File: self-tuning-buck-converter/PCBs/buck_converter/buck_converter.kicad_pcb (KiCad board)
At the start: 2 copper layers, 91.2 x 82.6 mm, 54 parts, among them Q1 NMOS, U1 TLO84CN, U2 OPA2830, U3 LT1999-50, U4 LD1117V50, U6 ESP32-DEVKITC-32D, U7 IR2125, U8 MAX11644

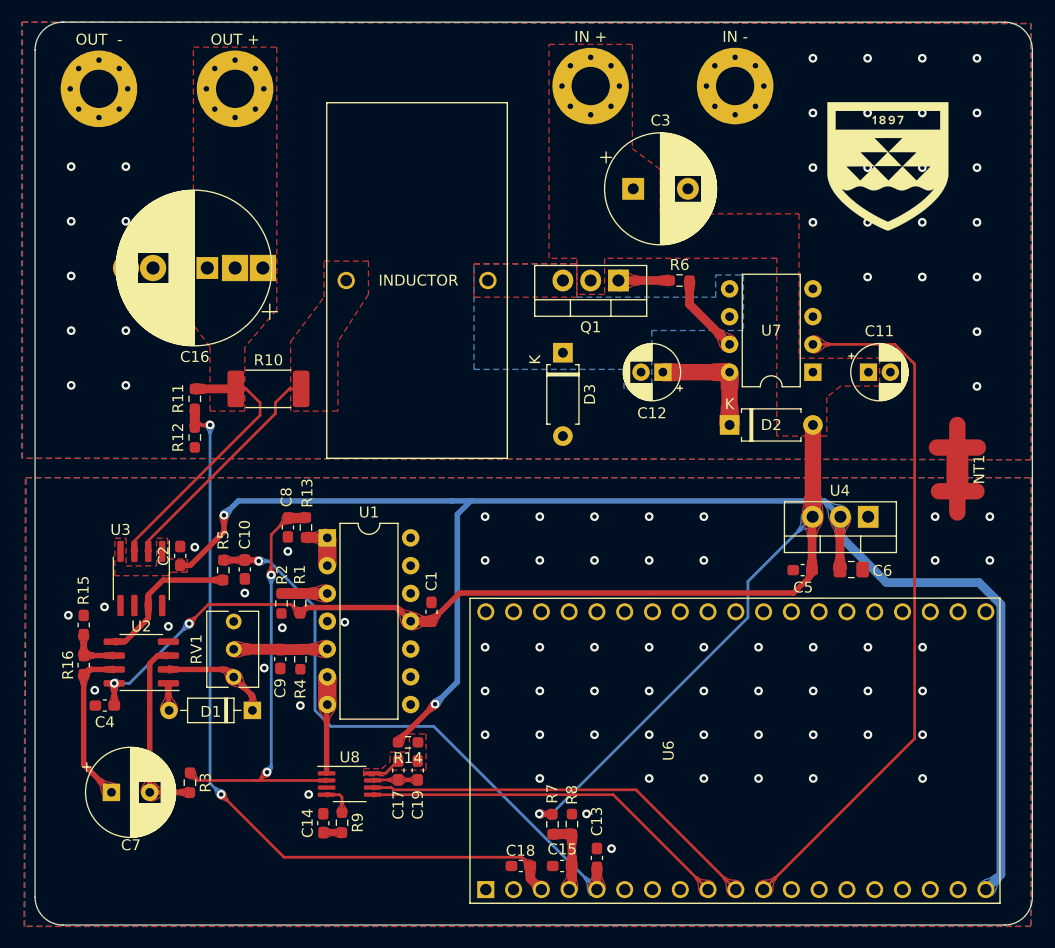
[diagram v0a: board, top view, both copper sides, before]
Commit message: removed un-necessay schematics
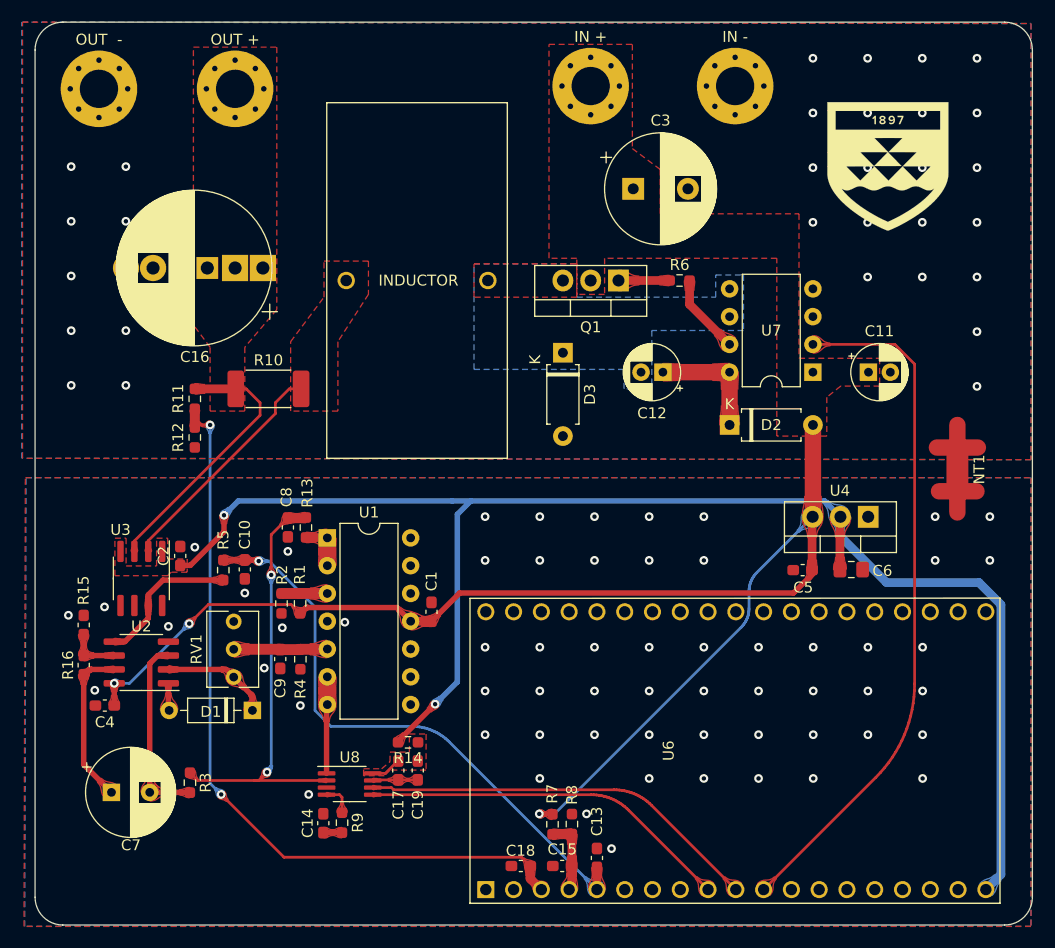
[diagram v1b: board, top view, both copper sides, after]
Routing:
- net PWM: track 63.8 -> 63.3 mm
